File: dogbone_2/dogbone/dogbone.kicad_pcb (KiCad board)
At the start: 2 copper layers, 23 x 27.4 mm, 11 parts, among them J1 jstsh4x1, U1 TLV2771CDBVT

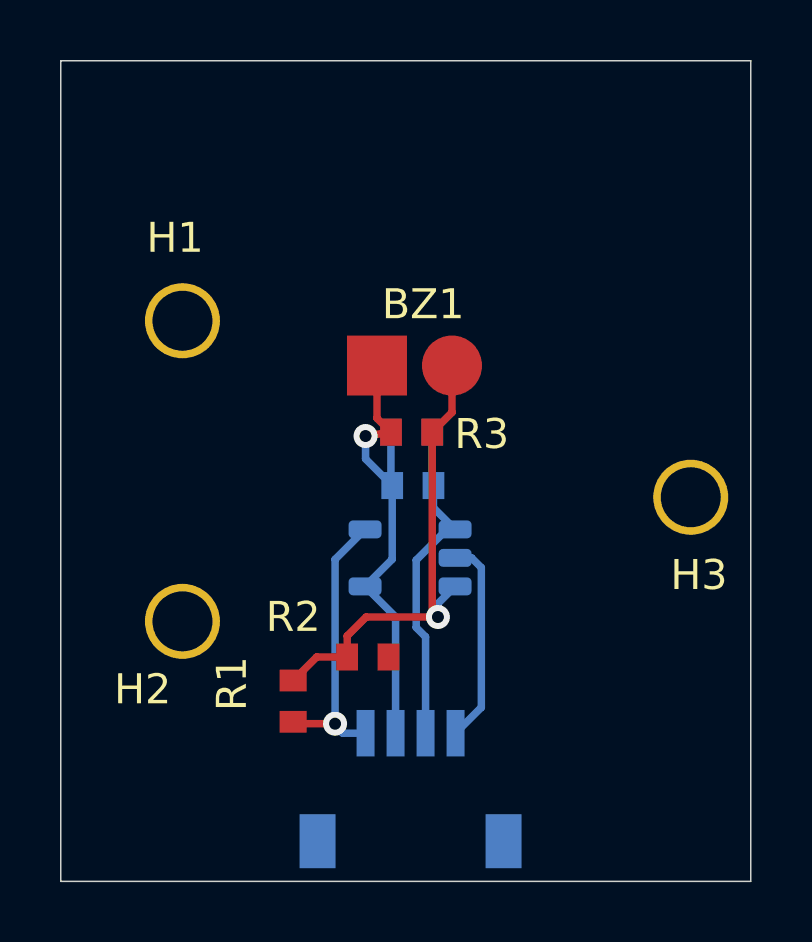
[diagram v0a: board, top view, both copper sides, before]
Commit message: updated dog bone schematic
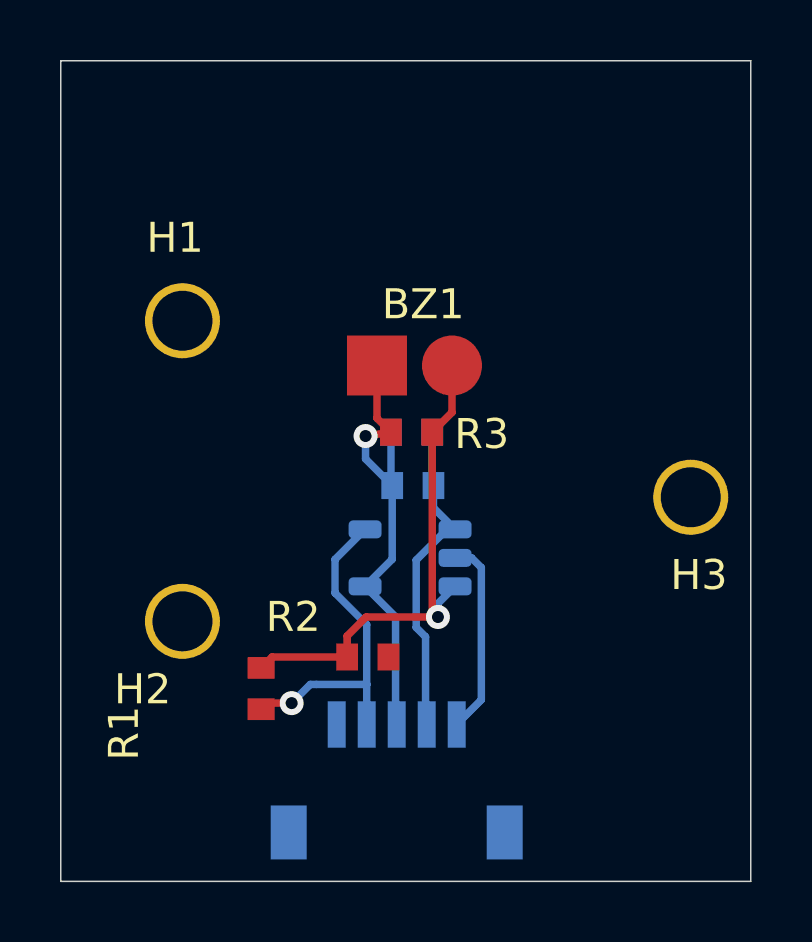
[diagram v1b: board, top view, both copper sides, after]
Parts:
- J1: value jstsh4x1 -> jstsh5x1; footprint exocam_charge_amp:jstsh4x1 -> exocam_charge_amp:jstsh5x1
- moved R1 1.15 mm to (48.7, 96.4)
- moved J1 0.29 mm to (55.0, 95.7)
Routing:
- net +3V3: track 9.55 -> 11.2 mm
- net VGND: track 16.1 -> 17.0 mm
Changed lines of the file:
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@@
     (thickness 1.6)
     (drawings 4)
-    (tracks 47)
+    (tracks 53)
     (zones 0)
     (modules 11)
-    (nets 7)
+    (nets 8)
   )
   (page A4)
@@
   (net 5 +3V3)
   (net 6 GND)
+  (net 7 "Net-(J1-Pad6)")
   (net_class Default "This is the default net class."
     (clearance 0.2)
@@
     (add_net GND)
     (add_net "Net-(J1-Pad5)")
+    (add_net "Net-(J1-Pad6)")
     (add_net UNAMP)
     (add_net VGND)
+  )
+  (module exocam_charge_amp:jstsh5x1 (layer B.Cu)
+    (at 54.9656 95.6564 180)
+    (fp_text reference J1 (at -5.9944 -4.1148) (layer B.SilkS)
+      (effects (font (size 1 1) (thickness 0.15)) (justify mirror))
+    )
+    (fp_text value jstsh5x1 (at 0 0.5) (layer B.Fab)
+      (effects (font (size 1 1) (thickness 0.15)) (justify mirror))
+    )
+    (fp_line (start -4.805 -6.84) (end 3.185 -6.84) (layer Dwgs.User) (width 0.12))
+    (fp_line (start -4.805 -6.84) (end -4.805 -3) (layer Dwgs.User) (width 0.12))
+    (fp_line (start 3.185 -3) (end -4.805 -3) (layer Dwgs.User) (width 0.12))
+    (fp_line (start 3.185 -3) (end 3.185 -6.84) (layer Dwgs.User) (width 0.12))
+    (pad 5 smd rect (at 1.19 -2.54 180) (size 0.6 1.55) (layers B.Cu B.Paste B.Mask)
+      (net 4 "Net-(J1-Pad5)"))
+    (pad 6 smd rect (at -4.41 -6.14 180) (size 1.2 1.8) (layers B.Cu B.Paste B.Mask)
+      (net 7 "Net-(J1-Pad6)"))
+    (pad 6 smd rect (at 2.79 -6.14 180) (size 1.2 1.8) (layers B.Cu B.Paste B.Mask)
+      (net 7 "Net-(J1-Pad6)"))
+    (pad 4 smd rect (at 0.19 -2.54 180) (size 0.6 1.55) (layers B.Cu B.Paste B.Mask)
+      (net 5 +3V3))
+    (pad 3 smd rect (at -0.81 -2.54 180) (size 0.6 1.55) (layers B.Cu B.Paste B.Mask)
+      (net 2 UNAMP))
+    (pad 2 smd rect (at -1.81 -2.54 180) (size 0.6 1.55) (layers B.Cu B.Paste B.Mask)
+      (net 3 AMP))
+    (pad 1 smd rect (at -2.81 -2.54 180) (size 0.6 1.55) (layers B.Cu B.Paste B.Mask)
+      (net 6 GND))
   )
   (module exocam_charge_amp:TLV2271DBV (layer B.Cu)
@@
   )
   (module exocam_charge_amp:0603_R (layer F.Cu)
-    (at 49.784 96.8375 90)
-    (fp_text reference R1 (at 0 0.5 270) (layer F.SilkS)
+    (at 48.7172 96.4184 90)
+    (fp_text reference R1 (at -2.0701 -2.032 270) (layer F.SilkS)
       (effects (font (size 1 1) (thickness 0.15)))
     )
@@
     (pad 1 smd rect (at -1.27 2.54 90) (size 0.725 0.9) (layers F.Cu F.Paste F.Mask)
       (net 5 +3V3))
-  )
-  (module exocam_charge_amp:jstsh4x1 (layer B.Cu)
-    (at 54.9275 95.9485 180)
-    (fp_text reference J1 (at -1.27 -4.572) (layer B.SilkS)
-      (effects (font (size 1 1) (thickness 0.15)) (justify mirror))
-    )
-    (fp_text value jstsh4x1 (at -24.4475 -11.3665) (layer B.Fab)
-      (effects (font (size 1 1) (thickness 0.15)) (justify mirror))
-    )
-    (fp_line (start -4.805 -6.84) (end 2.185 -6.84) (layer Dwgs.User) (width 0.12))
-    (fp_line (start -4.805 -6.84) (end -4.805 -3) (layer Dwgs.User) (width 0.12))
-    (fp_line (start 2.185 -3) (end -4.805 -3) (layer Dwgs.User) (width 0.12))
-    (fp_line (start 2.185 -3) (end 2.185 -6.84) (layer Dwgs.User) (width 0.12))
-    (pad 5 smd rect (at -4.41 -6.14 180) (size 1.2 1.8) (layers B.Cu B.Paste B.Mask)
-      (net 4 "Net-(J1-Pad5)"))
-    (pad 5 smd rect (at 1.79 -6.14 180) (size 1.2 1.8) (layers B.Cu B.Paste B.Mask)
-      (net 4 "Net-(J1-Pad5)"))
-    (pad 4 smd rect (at 0.19 -2.54 180) (size 0.6 1.55) (layers B.Cu B.Paste B.Mask)
-      (net 5 +3V3))
-    (pad 3 smd rect (at -0.81 -2.54 180) (size 0.6 1.55) (layers B.Cu B.Paste B.Mask)
-      (net 2 UNAMP))
-    (pad 2 smd rect (at -1.81 -2.54 180) (size 0.6 1.55) (layers B.Cu B.Paste B.Mask)
-      (net 3 AMP))
-    (pad 1 smd rect (at -2.81 -2.54 180) (size 0.6 1.55) (layers B.Cu B.Paste B.Mask)
-      (net 6 GND))
   )
   (module exocam_charge_amp:0603_R (layer B.Cu)
@@
   (gr_line (start 44.577 76.073) (end 67.577 76.073) (layer Edge.Cuts) (width 0.05))
   (gr_line (start 44.577 76.073) (end 44.577 103.427) (layer Edge.Cuts) (width 0.05))
-  (segment (start 53.108 95.9485) (end 52.324 96.7325) (width 0.25) (layer F.Cu) (net 1))
-  (segment (start 54.124 95.9485) (end 53.108 95.9485) (width 0.25) (layer F.Cu) (net 1))
   (segment (start 54.124 95.2485) (end 54.7575 94.615) (width 0.25) (layer F.Cu) (net 1))
   (segment (start 54.124 95.9485) (end 54.124 95.2485) (width 0.25) (layer F.Cu) (net 1))
@@
   (segment (start 56.9595 94.4245) (end 57.15 94.615) (width 0.25) (layer F.Cu) (net 1))
   (segment (start 56.9595 88.4555) (end 56.9595 94.4245) (width 0.25) (layer F.Cu) (net 1))
+  (segment (start 51.6221 95.9485) (end 51.2572 96.3134) (width 0.25) (layer F.Cu) (net 1))
+  (segment (start 54.124 95.9485) (end 51.6221 95.9485) (width 0.25) (layer F.Cu) (net 1))
   (segment (start 55.5845 90.192) (end 55.626 90.2335) (width 0.25) (layer B.Cu) (net 2))
   (segment (start 55.5845 88.4555) (end 55.5845 90.192) (width 0.25) (layer B.Cu) (net 2))
@@
   (segment (start 55.626 90.2335) (end 55.626 92.6895) (width 0.25) (layer B.Cu) (net 2))
   (segment (start 55.7375 94.61) (end 54.7215 93.594) (width 0.25) (layer B.Cu) (net 2))
-  (segment (start 55.7375 98.4885) (end 55.7375 94.61) (width 0.25) (layer B.Cu) (net 2))
   (segment (start 55.118 87.989) (end 55.5845 88.4555) (width 0.25) (layer F.Cu) (net 2))
   (segment (start 55.118 86.233) (end 55.118 87.989) (width 0.25) (layer F.Cu) (net 2))
@@
   (segment (start 54.737 89.3445) (end 55.626 90.2335) (width 0.25) (layer B.Cu) (net 2))
   (segment (start 54.737 88.5825) (end 54.737 89.3445) (width 0.25) (layer B.Cu) (net 2))
+  (segment (start 55.7375 98.1583) (end 55.7756 98.1964) (width 0.25) (layer B.Cu) (net 2))
+  (segment (start 55.7375 94.61) (end 55.7375 98.1583) (width 0.25) (layer B.Cu) (net 2))
   (segment (start 56.9595 90.192) (end 57.001 90.2335) (width 0.25) (layer B.Cu) (net 3))
   (segment (start 56.9595 88.4555) (end 56.9595 90.192) (width 0.25) (layer B.Cu) (net 3))
@@
   (segment (start 56.424999 94.963001) (end 56.424999 92.718733) (width 0.25) (layer B.Cu) (net 3))
   (segment (start 56.7375 95.275502) (end 56.424999 94.963001) (width 0.25) (layer B.Cu) (net 3))
-  (segment (start 56.7375 98.4885) (end 56.7375 95.275502) (width 0.25) (layer B.Cu) (net 3))
-  (segment (start 54.7375 98.4885) (end 53.975 98.4885) (width 0.25) (layer B.Cu) (net 5))
-  (segment (start 53.975 98.4885) (end 53.721 98.171) (width 0.25) (layer B.Cu) (net 5))
-  (segment (start 53.721 98.171) (end 53.721 98.2345) (width 0.25) (layer B.Cu) (net 5))
-  (via (at 53.721 98.171) (size 0.8) (drill 0.4) (layers F.Cu B.Cu) (net 5))
-  (segment (start 52.3875 98.171) (end 52.324 98.1075) (width 0.25) (layer F.Cu) (net 5))
-  (segment (start 53.721 98.171) (end 52.3875 98.171) (width 0.25) (layer F.Cu) (net 5))
+  (segment (start 56.7375 98.1583) (end 56.7756 98.1964) (width 0.25) (layer B.Cu) (net 3))
+  (segment (start 56.7375 95.275502) (end 56.7375 98.1583) (width 0.25) (layer B.Cu) (net 3))
   (segment (start 53.721 92.6945) (end 54.7215 91.694) (width 0.25) (layer B.Cu) (net 5))
-  (segment (start 53.721 98.171) (end 53.721 92.6945) (width 0.25) (layer B.Cu) (net 5))
+  (segment (start 53.721 93.815268) (end 53.721 92.6945) (width 0.25) (layer B.Cu) (net 5))
+  (segment (start 54.7756 94.869868) (end 53.721 93.815268) (width 0.25) (layer B.Cu) (net 5))
+  (segment (start 54.7756 96.8624) (end 53.0992 96.8624) (width 0.25) (layer B.Cu) (net 5))
+  (segment (start 54.7756 98.1964) (end 54.7756 96.8624) (width 0.25) (layer B.Cu) (net 5))
+  (segment (start 54.7756 96.8624) (end 54.7756 94.869868) (width 0.25) (layer B.Cu) (net 5))
+  (segment (start 53.0992 96.8624) (end 52.896 96.8624) (width 0.25) (layer B.Cu) (net 5))
+  (segment (start 52.896 96.8624) (end 52.2732 97.4852) (width 0.25) (layer B.Cu) (net 5))
+  (segment (start 52.2732 97.4852) (end 52.2732 97.4852) (width 0.25) (layer B.Cu) (net 5))
+  (via (at 52.2732 97.4852) (size 0.8) (drill 0.4) (layers F.Cu B.Cu) (net 5))
+  (segment (start 51.4604 97.4852) (end 51.2572 97.6884) (width 0.25) (layer F.Cu) (net 5))
+  (segment (start 52.2732 97.4852) (end 51.4604 97.4852) (width 0.25) (layer F.Cu) (net 5))
   (segment (start 58.2715 92.644) (end 57.7215 92.644) (width 0.25) (layer B.Cu) (net 6))
   (segment (start 58.59651 92.96901) (end 58.2715 92.644) (width 0.25) (layer B.Cu) (net 6))
-  (segment (start 58.59651 97.62949) (end 58.59651 92.96901) (width 0.25) (layer B.Cu) (net 6))
-  (segment (start 57.7375 98.4885) (end 58.59651 97.62949) (width 0.25) (layer B.Cu) (net 6))
+  (segment (start 58.59651 97.37549) (end 57.7756 98.1964) (width 0.25) (layer B.Cu) (net 6))
+  (segment (start 58.59651 92.96901) (end 58.59651 97.37549) (width 0.25) (layer B.Cu) (net 6))
 )
